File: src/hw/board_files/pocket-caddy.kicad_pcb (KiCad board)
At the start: 4 copper layers, 100 x 100 mm, 99 parts, among them J1 USB_C_Receptacle_USB2.0_14P, J2 Screw_Terminal_01x03, J3 Conn_01x03_Pin, J4 Conn_01x03_Pin, J5 Conn_01x03_Pin, J6 Test_Points, J7 Conn_01x04, J8 Molex 104031-0811, Q1 PMOS, SW1 SW_PWR, SW2 RESET, SW3 BTN_2, SW4 BTN_1_BOOT, SW5 BTN_3, U1 FT234XD-R, U2 MCP73871, U3 TPS63031DSKR, U4 ESP32-C3-WROOM-02, U5 NEO-M9N, U6 BQ27427, U7 SHT30-DIS, Y1 32.768kHz

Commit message: Changed fuel gauge IC. Need to update component references and BOM.
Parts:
- removed C1: 100n, Capacitor_SMD:C_0603_1608Metric_Pad1.08x0.95mm_HandSolder
- removed C23: 1u, Capacitor_SMD:C_0603_1608Metric_Pad1.08x0.95mm_HandSolder
- removed J4, J5: Conn_01x03_Pin, Connector_PinHeader_2.54mm:PinHeader_1x03_P2.54mm_Vertical
- removed JP1 (x2), JP2: SolderJumper_Open, Jumper:SolderJumper-2_P1.3mm_Open_TrianglePad1.0x1.5mm
- removed R1, R4: 10k, Resistor_SMD:R_0603_1608Metric_Pad0.98x0.95mm_HandSolder
- removed TP8: ESP32RX_TP, TestPoint:TestPoint_Loop_D2.54mm_Drill1.5mm_Beaded
- removed TP9: ESP32TX_TP, TestPoint:TestPoint_Loop_D2.54mm_Drill1.5mm_Beaded
- removed U1: FT234XD-R, Package_DFN_QFN:DFN-12-1EP_3x3mm_P0.45mm_EP1.65x2.38mm
- removed U6: BQ27427, Package_BGA:Texas_DSBGA-9_1.62x1.58mm_Layout3x3_P0.5mm
- added R23: 1M, Resistor_SMD:R_0805_2012Metric_Pad1.20x1.40mm_HandSolder, F.Cu at (236.3, 94.1)
- added R24: 470k, Resistor_SMD:R_0805_2012Metric_Pad1.20x1.40mm_HandSolder, F.Cu at (236.3, 97.1)
- added U8: BQ27411DRZT-G1A, Package_SON:Texas_S-PDSO-N12, F.Cu at (241.7, 92.0)
- C13, C15: value TBD -> 18p
- C22: value 2u2 -> 1u
- R20: value 10k -> 1M; footprint Resistor_SMD:R_0603_1608Metric_Pad0.98x0.95mm_HandSolder -> Resistor_SMD:R_0805_2012Metric_Pad1.20x1.40mm_HandSolder
- R22: value 10k -> 10m
- moved H1 274.1 mm to (223.2, 80.0)
- moved R19 215.2 mm to (176.8, 120.2), turned to 90 degrees
- moved C20 213.6 mm to (174.6, 127.3), turned to 90 degrees
- moved H2 204.5 mm to (128.3, 64.4)
- moved J6 178.6 mm to (127.0, 132.5)
- moved U7 174.2 mm to (95.7, 73.2)
- moved C12 169.6 mm to (119.9, 104.8)
- moved SW2 160.9 mm to (114.3, 109.2)
- moved C21 134.1 mm to (88.5, 71.0)
- moved R21 134.1 mm to (88.5, 76.0)
- moved C4 50.5 mm to (236.3, 105.8), turned to 0 degrees
- moved C3 47.9 mm to (236.3, 102.7), turned to 0 degrees
- moved R22 40.3 mm to (240.8, 98.0), turned to 0 degrees
- moved NT1 37.3 mm to (235.6, 84.2)
- moved C22 36.0 mm to (240.8, 95.5), turned to 0 degrees
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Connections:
- C22 pad 2: Net-(U6-V_{DD}) -> +3V3
- R20 pad 1: +3V3 -> Net-(U8-TEST)
- R20 pad 2: Net-(U6-GPOUT) -> GND
- R22 pad 1: GND -> VBAT
- U4 pad 10: /SD_CS -> /SDA
- U4 pad 11: Net-(J4-Pin_2) -> /Microcontroller/BTN_2
- U4 pad 12: Net-(J5-Pin_2) -> /Microcontroller/BTN_3
- U4 pad 13: Net-(JP1-B) -> /Microcontroller/USB_D-
- U4 pad 14: Net-(JP2-B) -> /Microcontroller/USB_D+
- U4 pad 3: /SDA -> /SCL
- U4 pad 4: /SCL -> /SD_CS
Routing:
- net /SCL: track 6.93 -> 43.1 mm
- net /SD_CS: track 0.00 -> 23.2 mm, vias 0 -> 1
- net /SDA: track 6.76 -> 18.4 mm
- net /Microcontroller/USB_D+: track 2.09 -> 12.6 mm
- net /Microcontroller/USB_D-: track 2.10 -> 10.7 mm
- net Net-(U1-CBUS0): track 6.32 -> 0.00 mm
- net +3V3: track 29.9 -> 33.9 mm, vias 8 -> 9
- net Net-(J3-Pin_2): track 3.16 -> 0.00 mm
- net Net-(U1-~{RESET}): track 3.04 -> 0.00 mm
- net /USB-C and Power/USB0_D+: track 13.3 -> 11.6 mm
- net /USB-C and Power/USB0_D-: track 12.7 -> 10.9 mm
- net Net-(U1-3V3OUT): track 1.46 -> 0.00 mm, vias 1 -> 0
- net Net-(SW1-B): track 4.70 -> 6.15 mm
- net GND: vias 11 -> 10
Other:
- board size 100 x 100 mm -> 67.3 x 100 mm

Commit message: Layout progress. Made new footprint for inductor. Changed test  points to pads
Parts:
- removed TP11: GND, TestPoint:TestPoint_Loop_D2.54mm_Drill1.5mm_Beaded
- added TP12: PROG, TestPoint:TestPoint_Pad_D1.5mm, F.Cu at (225.2, 113.3)
- L1: footprint Inductor_SMD:L_Coilcraft_LPS3010 -> Project_Library:TDK_VLS3012_3.0x3.0mm
- TP1, TP10, TP2, TP3, TP4, TP5, TP6, TP7: footprint TestPoint:TestPoint_Loop_D2.54mm_Drill1.5mm_Beaded -> TestPoint:TestPoint_Pad_D1.5mm
- moved BT2 279.0 mm to (200.9, 102.3), turned to -135 degrees
- moved D6 235.4 mm to (201.2, 96.3), turned to 90 degrees
- moved TP5 171.6 mm to (138.8, 75.6)
- moved TP7 171.5 mm to (137.3, 84.7)
- moved TP6 171.5 mm to (138.8, 79.2)
- moved TP4 167.4 mm to (135.3, 79.2)
- moved TP3 167.3 mm to (135.3, 75.6)
- moved TP1 163.0 mm to (131.8, 75.6)
- moved TP2 159.3 mm to (131.8, 79.2)
- moved TP10 154.9 mm to (131.8, 84.7)
- moved U8 29.1 mm to (217.2, 107.7), turned to -90 degrees
- moved R22 28.7 mm to (214.1, 108.5), turned to -90 degrees
- moved D5 26.6 mm to (215.7, 68.6), turned to 0 degrees
- moved C22 25.0 mm to (217.2, 103.7), turned to 180 degrees
- moved R11 23.9 mm to (215.7, 70.7), turned to 0 degrees
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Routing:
- net +3V3: track 33.9 -> 53.1 mm, vias 9 -> 29
- net Net-(BT2-+): track 0.00 -> 13.9 mm, vias 0 -> 1
- net Net-(AE1-FEED): track 1.74 -> 15.1 mm
- net Net-(U8-TEST): track 0.00 -> 11.2 mm
- net VBAT: track 0.00 -> 9.59 mm
- net Net-(U8-PROG): track 0.00 -> 8.01 mm
- net V_USB: track 17.1 -> 24.5 mm
- net GND: track 7.35 -> 14.3 mm
- net V_BCKP: track 0.00 -> 6.82 mm
- net Net-(Q1-S): track 0.00 -> 6.29 mm
- net Net-(SW1-B): track 6.15 -> 0.00 mm
- net V_SYS: track 1.62 -> 7.47 mm
- net Net-(U8-SRP): track 0.00 -> 4.79 mm
- net Net-(U3-EN): track 3.97 -> 6.63 mm
- net PGND: track 4.49 -> 2.47 mm
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- removed copper zone on F.Cu, net Net-(U3-EN)
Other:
- outline, holes or cut-outs redrawn
- board text added: "VB|VS"

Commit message: Nearly done with layout
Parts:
- removed H2: MountingHole_Pad, MountingHole:MountingHole_3.2mm_M3_Pad
- D6: footprint Package_TO_SOT_SMD:SOT-23-3 -> Package_TO_SOT_SMD:SOT-23_Handsoldering
- Q1: footprint Library:SOT91P240X110-3N_DMG2305UX-7 -> Package_TO_SOT_SMD:SOT-23_Handsoldering
- TP1: value SCL_TP -> SCL
- TP10: value VBCKP_TP -> VBCKP
- TP2: value SDA_TP -> SDA
- TP3: value SD_CS_TP -> CS
- TP4: value SPI_MOSI_TP -> MOSI
- TP5: value SPI_MISO_TP -> MISO
- TP6: value SPI_SCK_TP -> SCK
- TP7: value USB_PWR_TP -> VUSB
- moved J6 125.9 mm to (215.2, 42.7), turned to 0 degrees
- moved C21 123.3 mm to (205.3, 110.5), turned to 180 degrees
- moved R21 121.3 mm to (205.3, 108.6), turned to 180 degrees
- moved SW2 114.0 mm to (216.7, 59.0), turned to -90 degrees
- moved U7 105.3 mm to (201.1, 109.8)
- moved C12 104.3 mm to (212.3, 56.4), turned to 180 degrees
- moved TP10 69.6 mm to (200.9, 92.2)
- moved TP4 65.8 mm to (179.5, 127.9)
- moved TP5 62.2 mm to (179.5, 122.7)
- moved TP6 61.5 mm to (179.5, 125.3)
- moved TP3 61.5 mm to (169.3, 126.8)
- moved TP1 61.4 mm to (186.5, 103.5)
- moved TP2 58.9 mm to (186.5, 101.0), turned to 90 degrees
- moved TP7 39.0 mm to (176.3, 83.0), turned to 180 degrees
- moved NT1 19.2 mm to (217.5, 78.0)
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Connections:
- J6 pad 3: V_SYS -> VBAT
- J6 pad 4: V_SYS -> VBAT
- J6 pad 5: VBAT -> V_SYS
- J6 pad 6: VBAT -> V_SYS
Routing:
- net Net-(U4-EN): track 6.56 -> 96.3 mm, vias 0 -> 1
- net V_USB: track 24.5 -> 93.3 mm, vias 0 -> 2
- net VBAT: track 9.59 -> 71.9 mm
- net /Microcontroller/BTN_3: track 3.32 -> 63.9 mm, vias 0 -> 1
- net /SDA: track 19.3 -> 73.5 mm, vias 1 -> 3
- net V_SYS: track 7.47 -> 57.6 mm
- net /Microcontroller/BTN_2: track 3.32 -> 44.5 mm, vias 0 -> 1
- net /SCL: track 44.1 -> 82.7 mm, vias 1 -> 3
- net /Microcontroller/GPS_~{EN}: track 0.00 -> 32.3 mm, vias 0 -> 2
- net /Microcontroller/GPS_~{RESET}: track 0.00 -> 25.2 mm, vias 0 -> 2
- net /Microcontroller/BTN_1_BOOT: track 3.32 -> 17.2 mm
- net Net-(U8-PROG): track 8.01 -> 21.5 mm
- net GND: track 14.3 -> 23.8 mm, vias 10 -> 93
- net Net-(SW1-B): track 0.00 -> 8.71 mm
- net /SPI_MOSI: track 16.5 -> 23.5 mm, vias 1 -> 2
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- added copper zone on F.Cu, net V_SYS
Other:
- board size 67.3 x 100 mm -> 68 x 100 mm
- board text added: "+"
- board text added: "-"
- board text added: "3V3"
- board text added: "ANT"
- board text added: "B. Kuhn / B. York Oct 2025 Rev 0"
- board text added: "CR2032"
- board text added: "ESP32"
- board text added: "GND"
- board text added: "GPS Distance Measurer"
- board text added: "LiPo"
- board text added: "MicroSD"
- board text added: "NEO-M9N"
- board text added: "OFF"
- board text added: "ON"
- board text added: "Pocket Caddy"
- board text added: "RESET"
- board text added: "T"
- board text added: "TEMP"
- board text added: "TO DO: - Verify GND plane under antenna - Calculate 50 ohm trace width - Verify star GND point on regulator"
- board text added: "USB-C"
- board text added: "VBAT"
- board text added: "VSYS"
- board text added: "VS|VB"
- board text removed: "Figure out how to use net tie."
- board text removed: "VB|VS"

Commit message: Updated BOM
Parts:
- removed the R22 at (214.1, 108.5)
- added R19: 10m, Resistor_SMD:R_1206_3216Metric_Pad1.30x1.75mm_HandSolder, F.Cu at (214.1, 108.5)
- TP1: value SCL -> SCL_TP
- TP2: value SDA -> SDA_TP
- TP3: value CS -> SD_CS_TP
- TP4: value MOSI -> SPI_MOSI_TP
- TP5: value MISO -> SPI_MISO_TP
- TP6: value SCK -> SPI_SCK_TP
- TP7: value VUSB -> USB_PWR_TP
- TP8: renamed from TP10; value VBCKP -> VBCKP_TP
- renumbered C2 to C1, C11 to C10, C12 to C11, C14 to C12, C15 to C14, C17 to C15, C18 to C17, C19 to C18, C20 to C19, C3 to C2, C21 to C20, C22 to C21, C4 to C3, C5 to C4, C6 to C5, C7 to C6, C8 to C7, C9 to C8, C10 to C9, D2 to D1, D1 to D2, D7 to D6, D6 to D7, H3 to H2, H4 to H3, H5 to H4, J6 to J4, J7 to J5, J8 to J6, R2 to R1, R11 to R10, R13 to R11, R14 to R12, R15 to R13, R16 to R14, R17 to R15, R18 to R16, R19 to R17, R21 to R18, R7 to R2, R24 to R20, R23 to R21, R20 to R22, R8 to R4, R9 to R5, R5 to R6, R6 to R7, R10 to R8, R12 to R9, SW5 to SW4, SW4 to SW5, TP12 to TP9, U2 to U1, U3 to U2, U4 to U3, U5 to U4, U7 to U5, U8 to U6
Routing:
- net Net-(U6-SRP): track 4.79 -> 4.10 mm
- net VBAT: track 71.9 -> 71.4 mm
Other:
- board text added: "BOOT"

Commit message: Minor layout changes
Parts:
- TP3: value SD_CS_TP -> CS
- TP4: value SPI_MOSI_TP -> MOSI
- TP5: value SPI_MISO_TP -> MISO
- TP6: value SPI_SCK_TP -> SCK
- TP7: value USB_PWR_TP -> VUSB
- TP8: value VBCKP_TP -> VBCKP
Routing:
- net GND: track 23.8 -> 25.3 mm, vias 93 -> 177
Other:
- outline, holes or cut-outs redrawn

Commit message: Finish adding tags
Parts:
- added G***: LOGO, Project_Library:Coat of Arms Logo, F.Cu at (214.1, 39.5)
- added G***: LOGO, Project_Library:bradysTag_3.5mm, F.Cu at (208.9, 125.9)
- TP1: value SCL_TP -> SCL
- TP2: value SDA_TP -> SDA
- moved J4 2.11 mm to (215.4, 44.8)
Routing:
- net V_SYS: track 57.6 -> 55.2 mm
- net VBAT: track 71.4 -> 70.0 mm
- net GND: vias 177 -> 189
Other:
- outline, holes or cut-outs redrawn
- board text added: "TO DO: - Generate gerbers"
- board text removed: "ESP32"
- board text removed: "TO DO: - Verify GND plane under antenna - Calculate 50 ohm trace width - Verify star GND point on regulator"

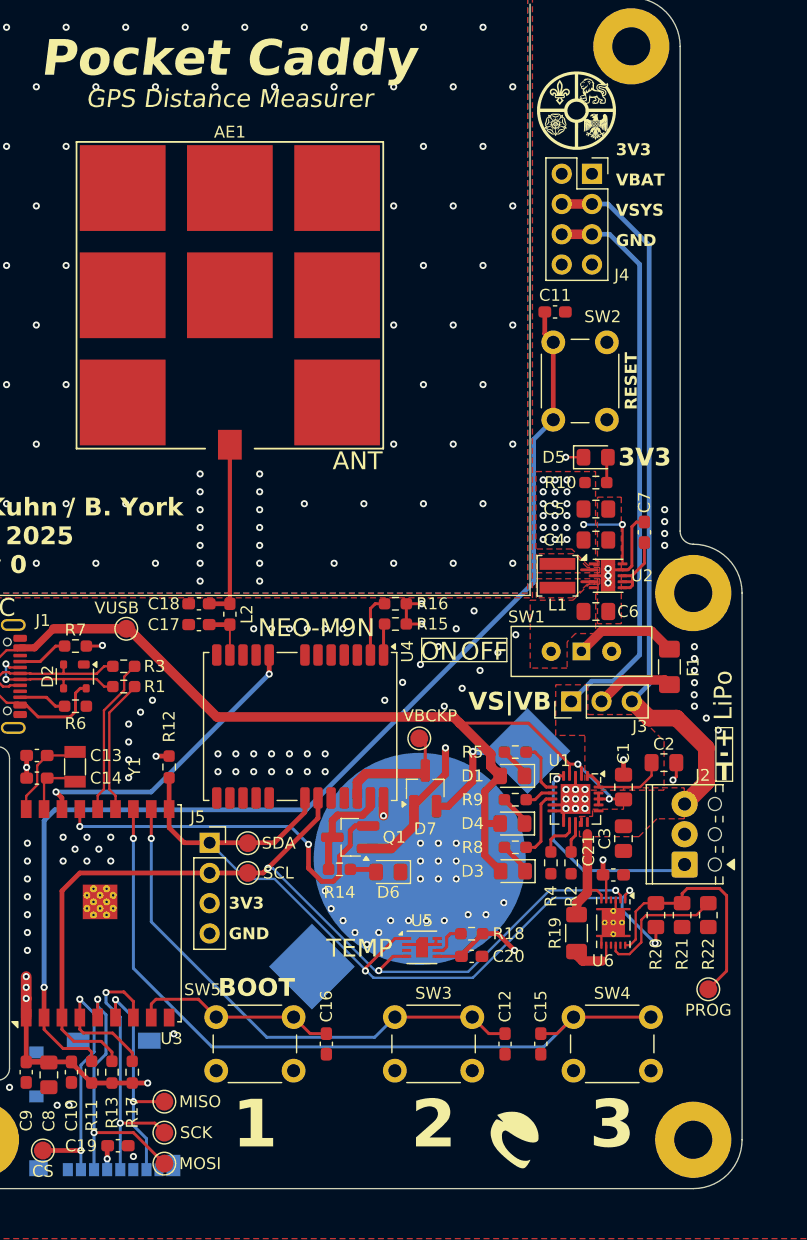
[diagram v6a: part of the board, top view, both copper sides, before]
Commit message: Updated terminal block PN, generated gerbers and zip file for submission
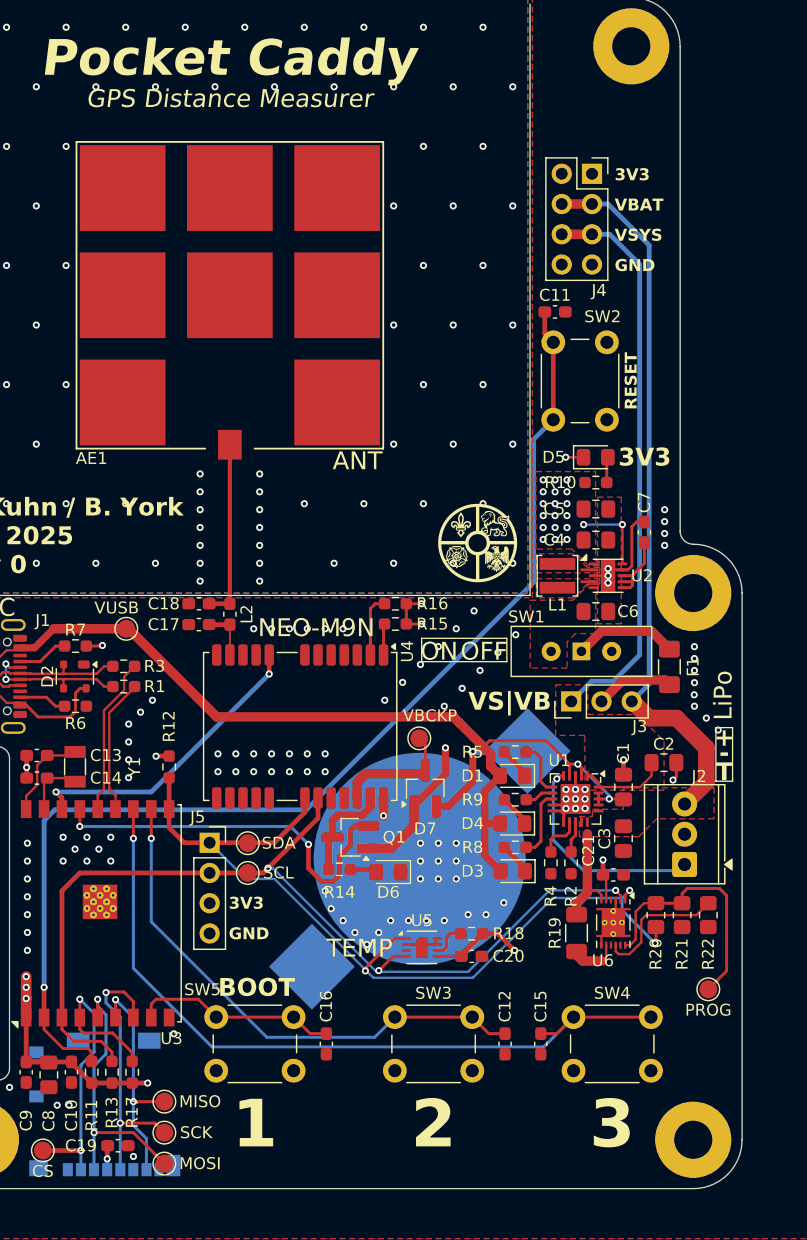
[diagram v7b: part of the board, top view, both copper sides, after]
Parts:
- J2: footprint TerminalBlock_Phoenix:TerminalBlock_Phoenix_MPT-0,5-3-2.54_1x03_P2.54mm_Horizontal -> TerminalBlock_TE-Connectivity:TerminalBlock_TE_282834-3_1x03_P2.54mm_Horizontal
- moved G*** 37.2 mm to (205.8, 75.8)
- moved G*** 17.2 mm to (224.6, 118.9)
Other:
- board text removed: "TO DO: - Generate gerbers"
